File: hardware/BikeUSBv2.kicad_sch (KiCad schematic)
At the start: 56 parts, among them J1 TYPE-C-31-M-16, J2 JST S2B-EH(LF)(SN), Q1 2SB772SQ, SW1 1TS002E-2500-2501-CT, SW2 1TS002E-2500-2501-CT, U1 TPS63070, U2 ATtiny1616-M, U3 FUSB302B10MPX, U4 HT7550, U5 TL431AIDBZR

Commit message: [PCB] LCSC Numbers
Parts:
- R6: LCSC (none) -> C218663
- R7: LCSC (none) -> C2831651
- U1: LCSC (none) -> C109322
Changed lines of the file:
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@@
+      (effects (font (size 1.27 1.27)) hide)
+    )
+    (property "LCSC" "C218663" (at 19.685 81.28 0)
       (effects (font (size 1.27 1.27)) hide)
     )
@@
     )
     (property "Datasheet" "~" (at 22.225 88.9 0)
+      (effects (font (size 1.27 1.27)) hide)
+    )
+    (property "LCSC" "C2831651" (at 19.685 88.9 0)
       (effects (font (size 1.27 1.27)) hide)
     )
@@
       (effects (font (size 1.27 1.27)) hide)
     )
+    (property "LCSC" "C109322" (at 168.275 59.69 0)
+      (effects (font (size 1.27 1.27)) hide)
+    )

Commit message: fix AC RDIV
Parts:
- R4: value 10k -> 27k; LCSC C217770 -> C375523
- R8: value 10k -> 3k; LCSC C217770 -> C218519
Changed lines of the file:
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@@
       (effects (font (size 1.27 1.27)))
     )
-    (property "Value" "10k" (at 71.12 116.205 90)
+    (property "Value" "27k" (at 71.12 116.205 90)
       (effects (font (size 1.27 1.27)))
     )
@@
       (effects (font (size 1.27 1.27)) hide)
     )
-    (property "LCSC" "C217770" (at 68.58 116.205 0)
+    (property "LCSC" "C375523" (at 71.12 116.205 90)
       (effects (font (size 1.27 1.27)) hide)
     )
@@
       (effects (font (size 1.27 1.27)))
     )
-    (property "Value" "10k" (at 71.12 123.825 90)
+    (property "Value" "3k" (at 71.12 123.825 90)
       (effects (font (size 1.27 1.27)))
     )
@@
       (effects (font (size 1.27 1.27)) hide)
     )
-    (property "LCSC" "C217770" (at 68.58 123.825 0)
-      (effects (font (size 1.27 1.27)) hide)
-    )
+    (property "LCSC" "C218519" (at 68.58 123.825 0)
+      (effects (font (size 1.27 1.27)) hide)
+    )

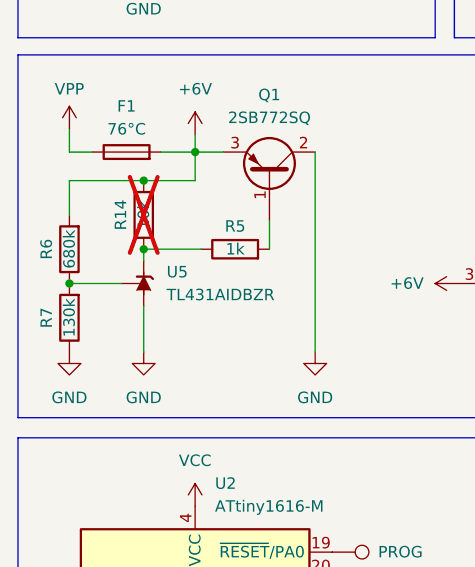
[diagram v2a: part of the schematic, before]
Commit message: [PCB] fix resistors
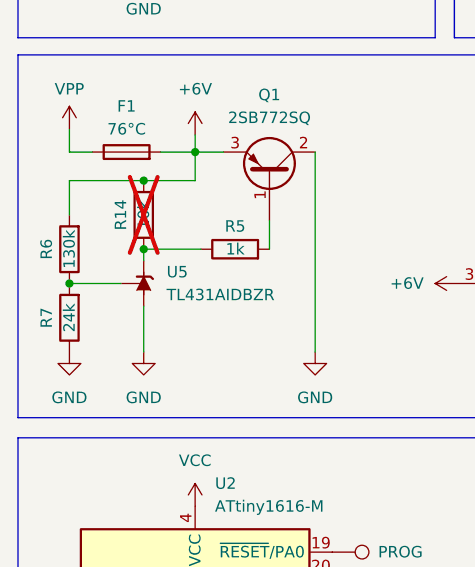
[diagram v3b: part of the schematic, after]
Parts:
- R6: value 680k -> 130k; LCSC C218663 -> C2831651
- R7: value 130k -> 24k; LCSC C2831651 -> C218452
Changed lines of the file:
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@@
       (effects (font (size 1.27 1.27)))
     )
-    (property "Value" "680k" (at 22.225 81.28 90)
+    (property "Value" "130k" (at 22.225 81.28 90)
       (effects (font (size 1.27 1.27)))
     )
@@
       (effects (font (size 1.27 1.27)) hide)
     )
-    (property "LCSC" "C218663" (at 19.685 81.28 0)
+    (property "LCSC" "C2831651" (at 19.685 81.28 0)
       (effects (font (size 1.27 1.27)) hide)
     )
@@
       (effects (font (size 1.27 1.27)))
     )
-    (property "Value" "130k" (at 22.225 88.9 90)
+    (property "Value" "24k" (at 22.225 88.9 90)
       (effects (font (size 1.27 1.27)))
     )
@@
       (effects (font (size 1.27 1.27)) hide)
     )
-    (property "LCSC" "C2831651" (at 19.685 88.9 0)
-      (effects (font (size 1.27 1.27)) hide)
-    )
+    (property "LCSC" "C218452" (at 19.685 88.9 0)
+      (effects (font (size 1.27 1.27)) hide)
+    )

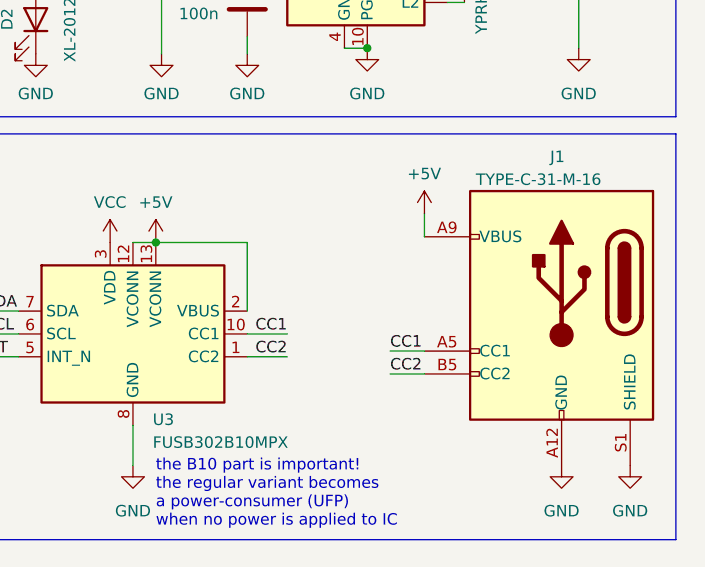
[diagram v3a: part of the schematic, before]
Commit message: [PCB] add CC testpads
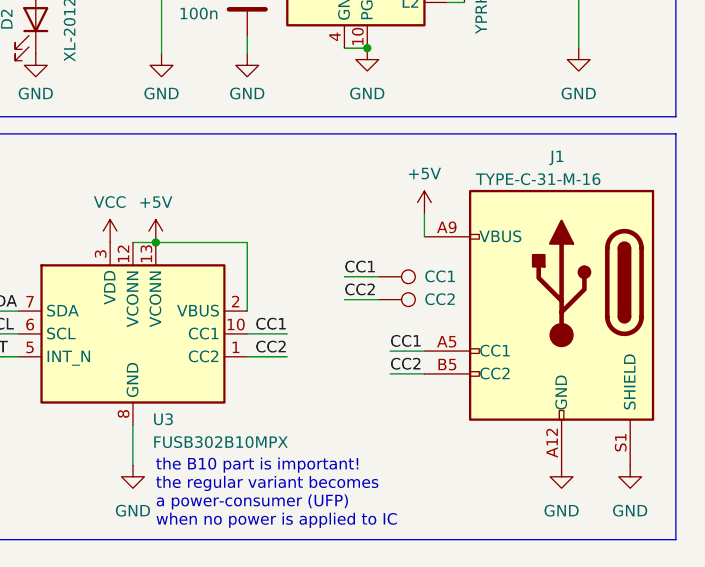
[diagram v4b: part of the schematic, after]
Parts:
- added TP7: CC1, TestPoint:TestPoint_Pad_D1.5mm, symbol Connector:TestPoint
- added TP8: CC2, TestPoint:TestPoint_Pad_D1.5mm, symbol Connector:TestPoint
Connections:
- net CC1: now also TP7.1
- net CC2: now also TP8.1
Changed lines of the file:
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@@
+    (stroke (width 0) (type default))
+  )
+  (wire (pts (xy 167.005 118.11) (xy 170.815 118.11))
     (stroke (width 0) (type default))
   )
@@
   )
   (wire (pts (xy 146.685 77.47) (xy 146.685 80.01))
+    (stroke (width 0) (type default))
+  )
+  (wire (pts (xy 167.005 120.65) (xy 170.815 120.65))
     (stroke (width 0) (type default))
   )
@@
     (effects (font (size 1.27 1.27)) (justify left bottom))
   )
+  (label "CC1" (at 167.005 118.11 0) (fields_autoplaced)
+    (effects (font (size 1.27 1.27)) (justify left bottom))
+  )
   (label "EN" (at 17.145 142.875 0) (fields_autoplaced)
     (effects (font (size 1.27 1.27)) (justify left bottom))
@@
   (label "CC1" (at 160.655 124.46 180) (fields_autoplaced)
     (effects (font (size 1.27 1.27)) (justify right bottom))
+  )
+  (label "CC2" (at 167.005 120.65 0) (fields_autoplaced)
+    (effects (font (size 1.27 1.27)) (justify left bottom))
   )
   (label "FUSB_INT" (at 61.595 125.095 180) (fields_autoplaced)
@@
     )
   )
+  (symbol (lib_id "Connector:TestPoint") (at 170.815 120.65 270) (unit 1)
+    (in_bom no) (on_board yes) (dnp no)
+    (property "Reference" "TP8" (at 177.165 119.38 90)
+      (effects (font (size 1.27 1.27)) (justify left) hide)
+    )
+    (property "Value" "CC2" (at 175.895 120.65 90)
+      (effects (font (size 1.27 1.27)) (justify left))
+    )
+    (property "Footprint" "TestPoint:TestPoint_Pad_D1.5mm" (at 170.815 125.73 0)
+      (effects (font (size 1.27 1.27)) hide)
+    )
+    (property "Datasheet" "~" (at 170.815 125.73 0)
+      (effects (font (size 1.27 1.27)) hide)
+    )
+    (pin "1")
+    (instances
+      (project "BikeUSBv2"
+        (path "/b4aff538-5116-4944-9d24-c26a88d7dfe8"
+          (reference "TP8") (unit 1)
+        )
+      )
+    )
+  )
   (symbol (lib_id "power:GND") (at 191.135 139.065 0) (mirror y) (unit 1)
     (in_bom yes) (on_board yes) (dnp no) (fields_autoplaced)
@@
         )
       )
+    )
+  )
+  (symbol (lib_id "Connector:TestPoint") (at 170.815 118.11 270) (unit 1)
+    (in_bom no) (on_board yes) (dnp no)
+    (property "Reference" "TP7" (at 175.895 116.84 90)
+      (effects (font (size 1.27 1.27)) (justify left) hide)
+    )
+    (property "Value" "CC1" (at 175.895 118.11 90)
+      (effects (font (size 1.27 1.27)) (justify left))
+    )
+    (property "Footprint" "TestPoint:TestPoint_Pad_D1.5mm" (at 170.815 123.19 0)
+      (effects (font (size 1.27 1.27)) hide)
+    )
+    (property "Datasheet" "~" (at 170.815 123.19 0)
+      (effects (font (size 1.27 1.27)) hide)
+    )
+    (pin "1")
+    (instances
+      (project "BikeUSBv2"
+        (path "/b4aff538-5116-4944-9d24-c26a88d7dfe8"
+          (reference "TP7") (unit 1)
+        )
+      )

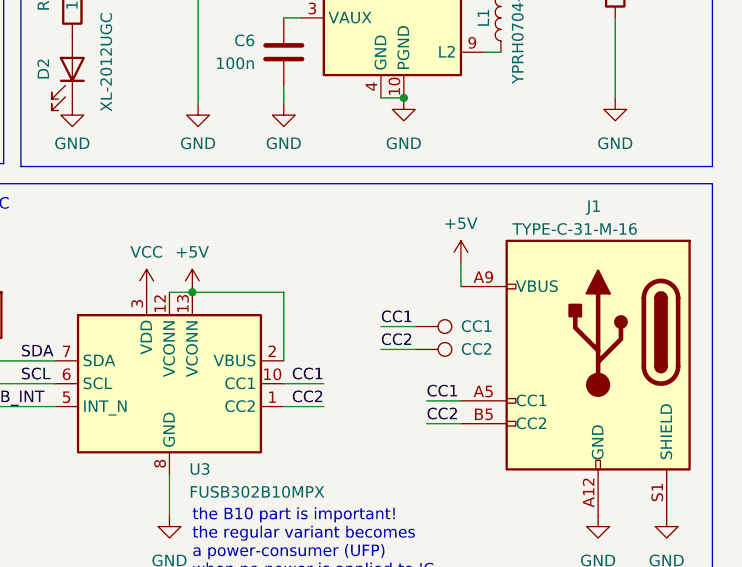
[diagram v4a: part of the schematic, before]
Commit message: [PCB] add I2C testpads and improve groundplane
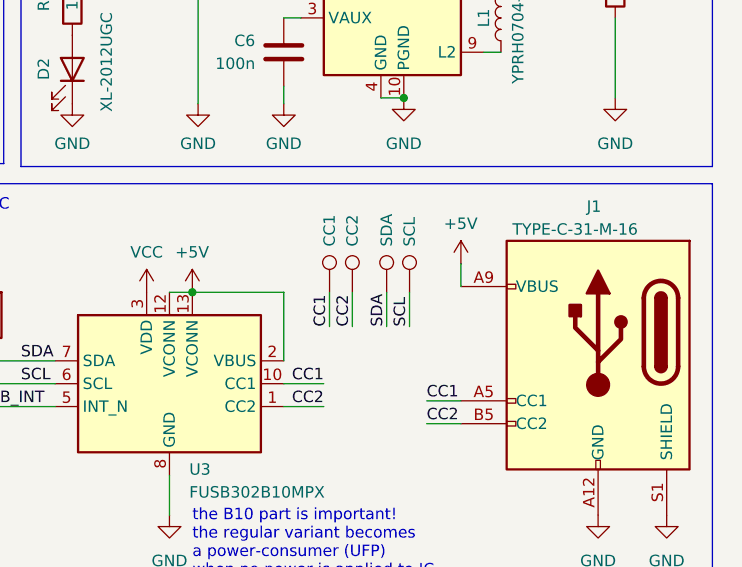
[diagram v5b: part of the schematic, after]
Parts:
- added TP10: SCL, TestPoint:TestPoint_Pad_D1.5mm, symbol Connector:TestPoint
- added TP9: SDA, TestPoint:TestPoint_Pad_D1.5mm, symbol Connector:TestPoint
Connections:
- net SCL: now also TP10.1
- net SDA: now also TP9.1
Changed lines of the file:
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@@
     (stroke (width 0) (type default))
   )
-  (wire (pts (xy 167.005 118.11) (xy 170.815 118.11))
+  (wire (pts (xy 161.29 118.11) (xy 161.29 114.3))
     (stroke (width 0) (type default))
   )
@@
     (stroke (width 0) (type default))
   )
-  (wire (pts (xy 167.005 120.65) (xy 170.815 120.65))
+  (wire (pts (xy 163.83 118.11) (xy 163.83 114.3))
     (stroke (width 0) (type default))
   )
@@
     (stroke (width 0) (type default))
   )
+  (wire (pts (xy 170.18 118.11) (xy 170.18 114.3))
+    (stroke (width 0) (type default))
+  )
   (wire (pts (xy 187.325 76.2) (xy 193.04 76.2))
     (stroke (width 0) (type default))
@@
   )
   (wire (pts (xy 156.21 121.92) (xy 156.21 114.3))
+    (stroke (width 0) (type default))
+  )
+  (wire (pts (xy 167.64 118.11) (xy 167.64 114.3))
     (stroke (width 0) (type default))
   )
@@
     (effects (font (size 1.27 1.27)) (justify left bottom))
   )
+  (label "SCL" (at 170.18 118.11 90) (fields_autoplaced)
+    (effects (font (size 1.27 1.27)) (justify left bottom))
+  )
   (label "CC2" (at 172.085 128.905 0) (fields_autoplaced)
     (effects (font (size 1.27 1.27)) (justify left bottom))
   )
-  (label "CC1" (at 167.005 118.11 0) (fields_autoplaced)
+  (label "CC1" (at 161.29 118.11 90) (fields_autoplaced)
     (effects (font (size 1.27 1.27)) (justify left bottom))
   )
@@
     (effects (font (size 1.27 1.27)) (justify right bottom))
   )
-  (label "CC2" (at 167.005 120.65 0) (fields_autoplaced)
+  (label "SDA" (at 167.64 118.11 90) (fields_autoplaced)
+    (effects (font (size 1.27 1.27)) (justify left bottom))
+  )
+  (label "CC2" (at 163.83 118.11 90) (fields_autoplaced)
     (effects (font (size 1.27 1.27)) (justify left bottom))
   )
@@
     )
   )
-  (symbol (lib_id "Connector:TestPoint") (at 170.815 120.65 270) (unit 1)
+  (symbol (lib_id "Connector:TestPoint") (at 163.83 114.3 0) (unit 1)
     (in_bom no) (on_board yes) (dnp no)
-    (property "Reference" "TP8" (at 177.165 119.38 90)
+    (property "Reference" "TP8" (at 162.56 107.95 90)
       (effects (font (size 1.27 1.27)) (justify left) hide)
     )
-    (property "Value" "CC2" (at 175.895 120.65 90)
-      (effects (font (size 1.27 1.27)) (justify left))
-    )
-    (property "Footprint" "TestPoint:TestPoint_Pad_D1.5mm" (at 170.815 125.73 0)
-      (effects (font (size 1.27 1.27)) hide)
-    )
-    (property "Datasheet" "~" (at 170.815 125.73 0)
+    (property "Value" "CC2" (at 163.83 109.22 90)
+      (effects (font (size 1.27 1.27)) (justify left))
+    )
+    (property "Footprint" "TestPoint:TestPoint_Pad_D1.5mm" (at 168.91 114.3 0)
+      (effects (font (size 1.27 1.27)) hide)
+    )
+    (property "Datasheet" "~" (at 168.91 114.3 0)
       (effects (font (size 1.27 1.27)) hide)
     )
@@
         (path "/b4aff538-5116-4944-9d24-c26a88d7dfe8"
           (reference "#PWR02") (unit 1)
+        )
+      )
+    )
+  )
+  (symbol (lib_id "Connector:TestPoint") (at 167.64 114.3 0) (unit 1)
+    (in_bom no) (on_board yes) (dnp no)
+    (property "Reference" "TP9" (at 166.37 109.22 90)
+      (effects (font (size 1.27 1.27)) (justify left) hide)
+    )
+    (property "Value" "SDA" (at 167.64 109.22 90)
+      (effects (font (size 1.27 1.27)) (justify left))
+    )
+    (property "Footprint" "TestPoint:TestPoint_Pad_D1.5mm" (at 172.72 114.3 0)
+      (effects (font (size 1.27 1.27)) hide)
+    )
+    (property "Datasheet" "~" (at 172.72 114.3 0)
+      (effects (font (size 1.27 1.27)) hide)
+    )
+    (pin "1")
+    (instances
+      (project "BikeUSBv2"
+        (path "/b4aff538-5116-4944-9d24-c26a88d7dfe8"
+          (reference "TP9") (unit 1)
         )
       )
@@
     )
   )
-  (symbol (lib_id "Connector:TestPoint") (at 170.815 118.11 270) (unit 1)
+  (symbol (lib_id "Connector:TestPoint") (at 161.29 114.3 0) (unit 1)
     (in_bom no) (on_board yes) (dnp no)
-    (property "Reference" "TP7" (at 175.895 116.84 90)
+    (property "Reference" "TP7" (at 160.02 109.22 90)
       (effects (font (size 1.27 1.27)) (justify left) hide)
     )
-    (property "Value" "CC1" (at 175.895 118.11 90)
-      (effects (font (size 1.27 1.27)) (justify left))
-    )
-    (property "Footprint" "TestPoint:TestPoint_Pad_D1.5mm" (at 170.815 123.19 0)
-      (effects (font (size 1.27 1.27)) hide)
-    )
-    (property "Datasheet" "~" (at 170.815 123.19 0)
+    (property "Value" "CC1" (at 161.29 109.22 90)
+      (effects (font (size 1.27 1.27)) (justify left))
+    )
+    (property "Footprint" "TestPoint:TestPoint_Pad_D1.5mm" (at 166.37 114.3 0)
+      (effects (font (size 1.27 1.27)) hide)
+    )
+    (property "Datasheet" "~" (at 166.37 114.3 0)
       (effects (font (size 1.27 1.27)) hide)
     )
@@
         )
       )
+    )
+  )
+  (symbol (lib_id "Connector:TestPoint") (at 170.18 114.3 0) (unit 1)
+    (in_bom no) (on_board yes) (dnp no)
+    (property "Reference" "TP10" (at 168.91 107.95 90)
+      (effects (font (size 1.27 1.27)) (justify left) hide)
+    )
+    (property "Value" "SCL" (at 170.18 109.22 90)
+      (effects (font (size 1.27 1.27)) (justify left))
+    )
+    (property "Footprint" "TestPoint:TestPoint_Pad_D1.5mm" (at 175.26 114.3 0)
+      (effects (font (size 1.27 1.27)) hide)
+    )
+    (property "Datasheet" "~" (at 175.26 114.3 0)
+      (effects (font (size 1.27 1.27)) hide)
+    )
+    (pin "1")
+    (instances
+      (project "BikeUSBv2"
+        (path "/b4aff538-5116-4944-9d24-c26a88d7dfe8"
+          (reference "TP10") (unit 1)
+        )
+      )

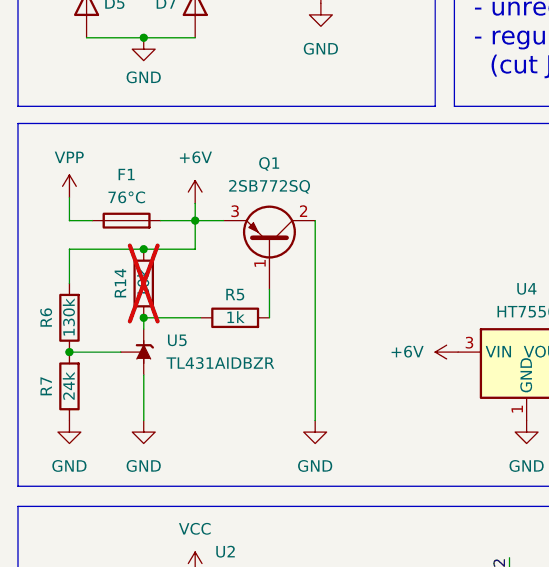
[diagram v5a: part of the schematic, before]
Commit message: [PCB] add pullup-resistor for TL431
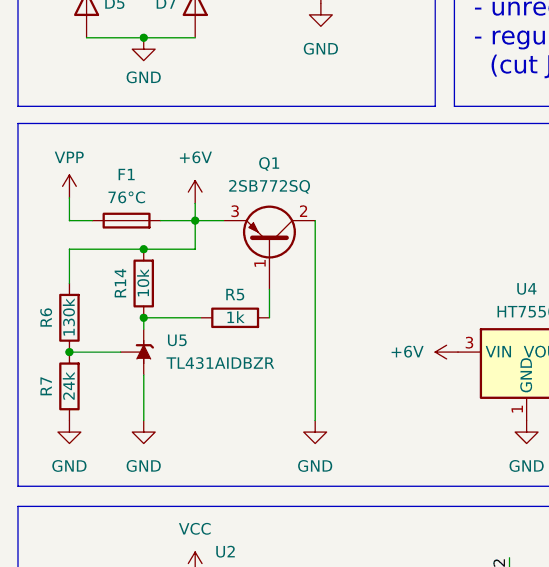
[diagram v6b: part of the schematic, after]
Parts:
- R14: now fitted
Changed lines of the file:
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@@
   )
   (symbol (lib_id "Device:R") (at 30.48 77.47 180) (unit 1)
-    (in_bom yes) (on_board no) (dnp yes)
+    (in_bom yes) (on_board yes) (dnp no)
     (property "Reference" "R14" (at 27.94 77.47 90)
       (effects (font (size 1.27 1.27)))

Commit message: [PCB] minor fixes
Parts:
- R14: value 10k -> 1k; LCSC C217770 -> C110774
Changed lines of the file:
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@@
       (effects (font (size 1.27 1.27)))
     )
-    (property "Value" "10k" (at 30.48 77.47 90)
+    (property "Value" "1k" (at 30.48 77.47 90)
       (effects (font (size 1.27 1.27)))
     )
@@
       (effects (font (size 1.27 1.27)) hide)
     )
-    (property "LCSC" "C217770" (at 27.94 77.47 0)
+    (property "LCSC" "C110774" (at 27.94 77.47 0)
       (effects (font (size 1.27 1.27)) hide)
     )
